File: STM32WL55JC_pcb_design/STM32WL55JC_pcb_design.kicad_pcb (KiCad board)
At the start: 2 copper layers, 98 parts, among them IC1 CY8C9540A-24PVXIT, IC2 PE4259, IC3 HTS221TR, J1 Conn_01x03, J10 Conn_01x06_Male, J11 Conn_02x02_Odd_Even, J12 Conn_01x10, J13 Conn_01x10, J14 Conn_01x10, J15 Conn_01x10, J16 Conn_Coaxial, J17 CT3151-2, J18 CT3151-2, J19 USB_A, J2 Conn_01x03, J20 Conn_02x02_Odd_Even, J21 Conn_01x11_Male, J3 Conn_02x05_Odd_Even, J4 Conn_01x03, J5 Conn_01x09, J6 Conn_01x09, J7 Conn_01x03, J8 Conn_01x09, J9 Conn_01x09, Q1 AO3401A, SW1 SW_MEC_5E, SW2 SW_MEC_5E, U1 STM32WL55JCI7, U2 DS1307+, U3 L80-M39, U4 LIS3DHTR, U6 AMS1117-3.3, U7 AMS1117-5.0, Y1 32MHz, Y2 32.768kHz, Y3 32.768kHz

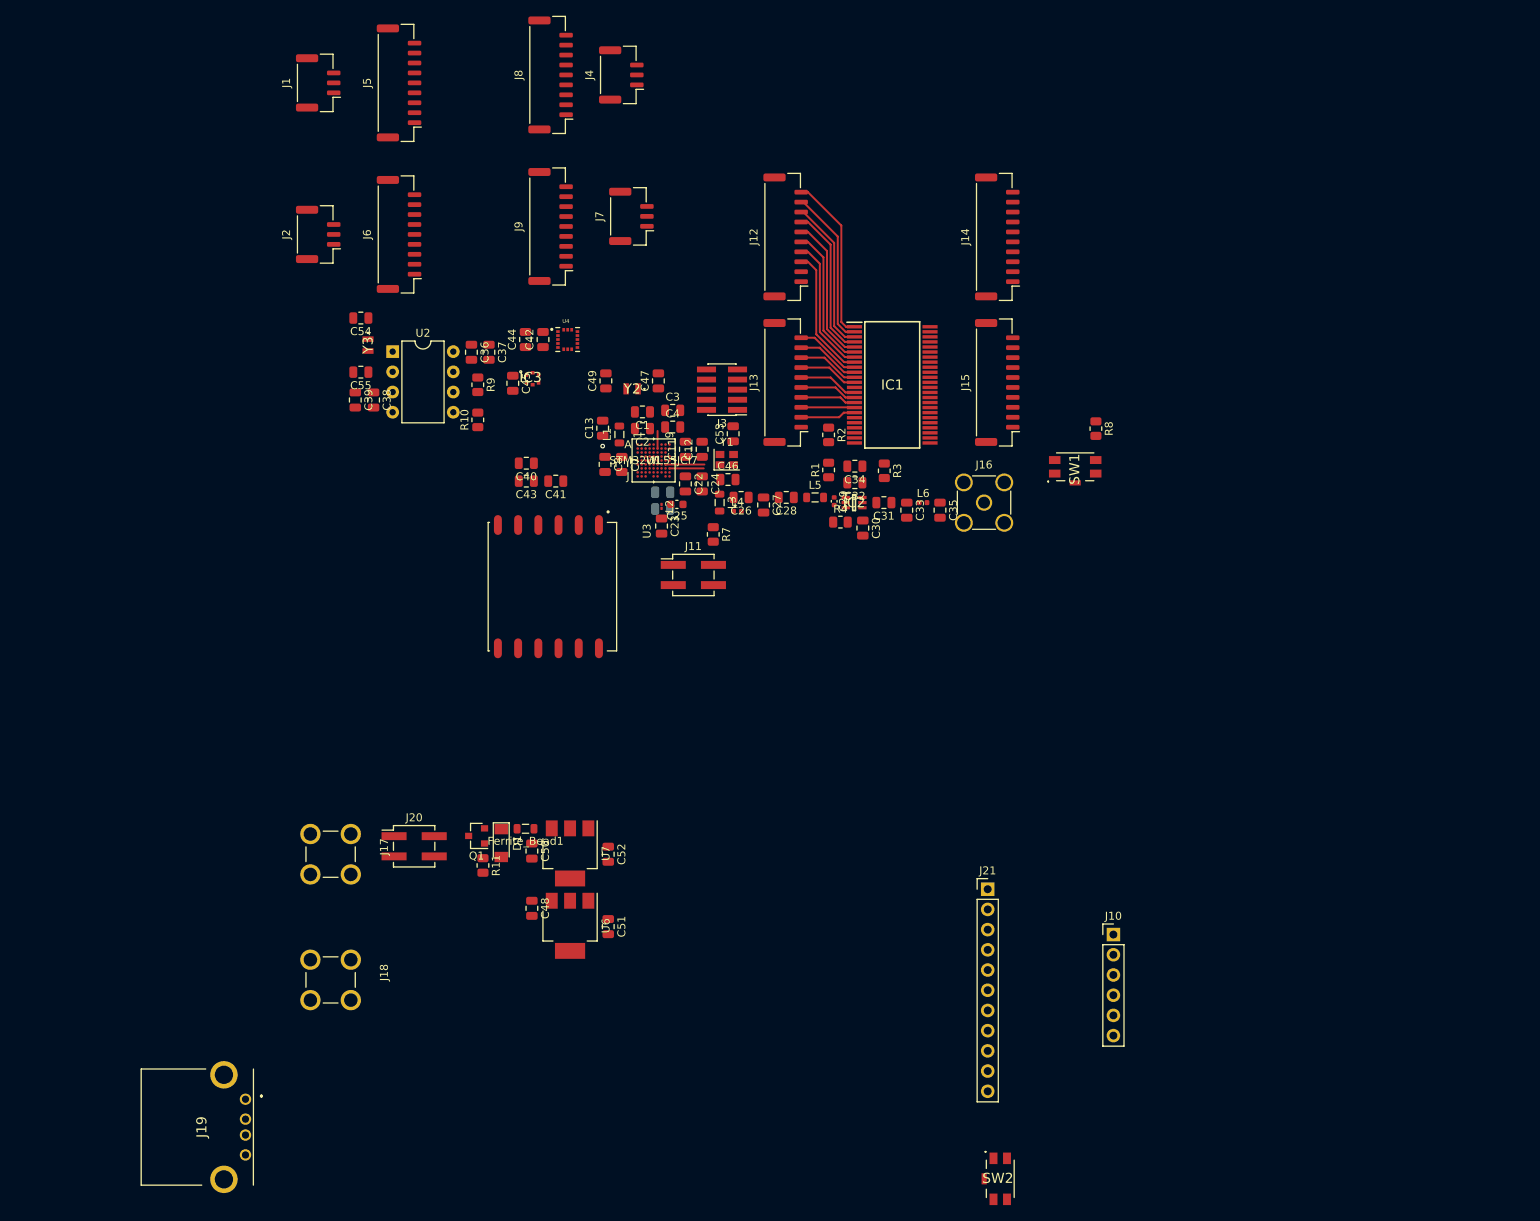
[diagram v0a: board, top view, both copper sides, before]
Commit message: Finished component placement
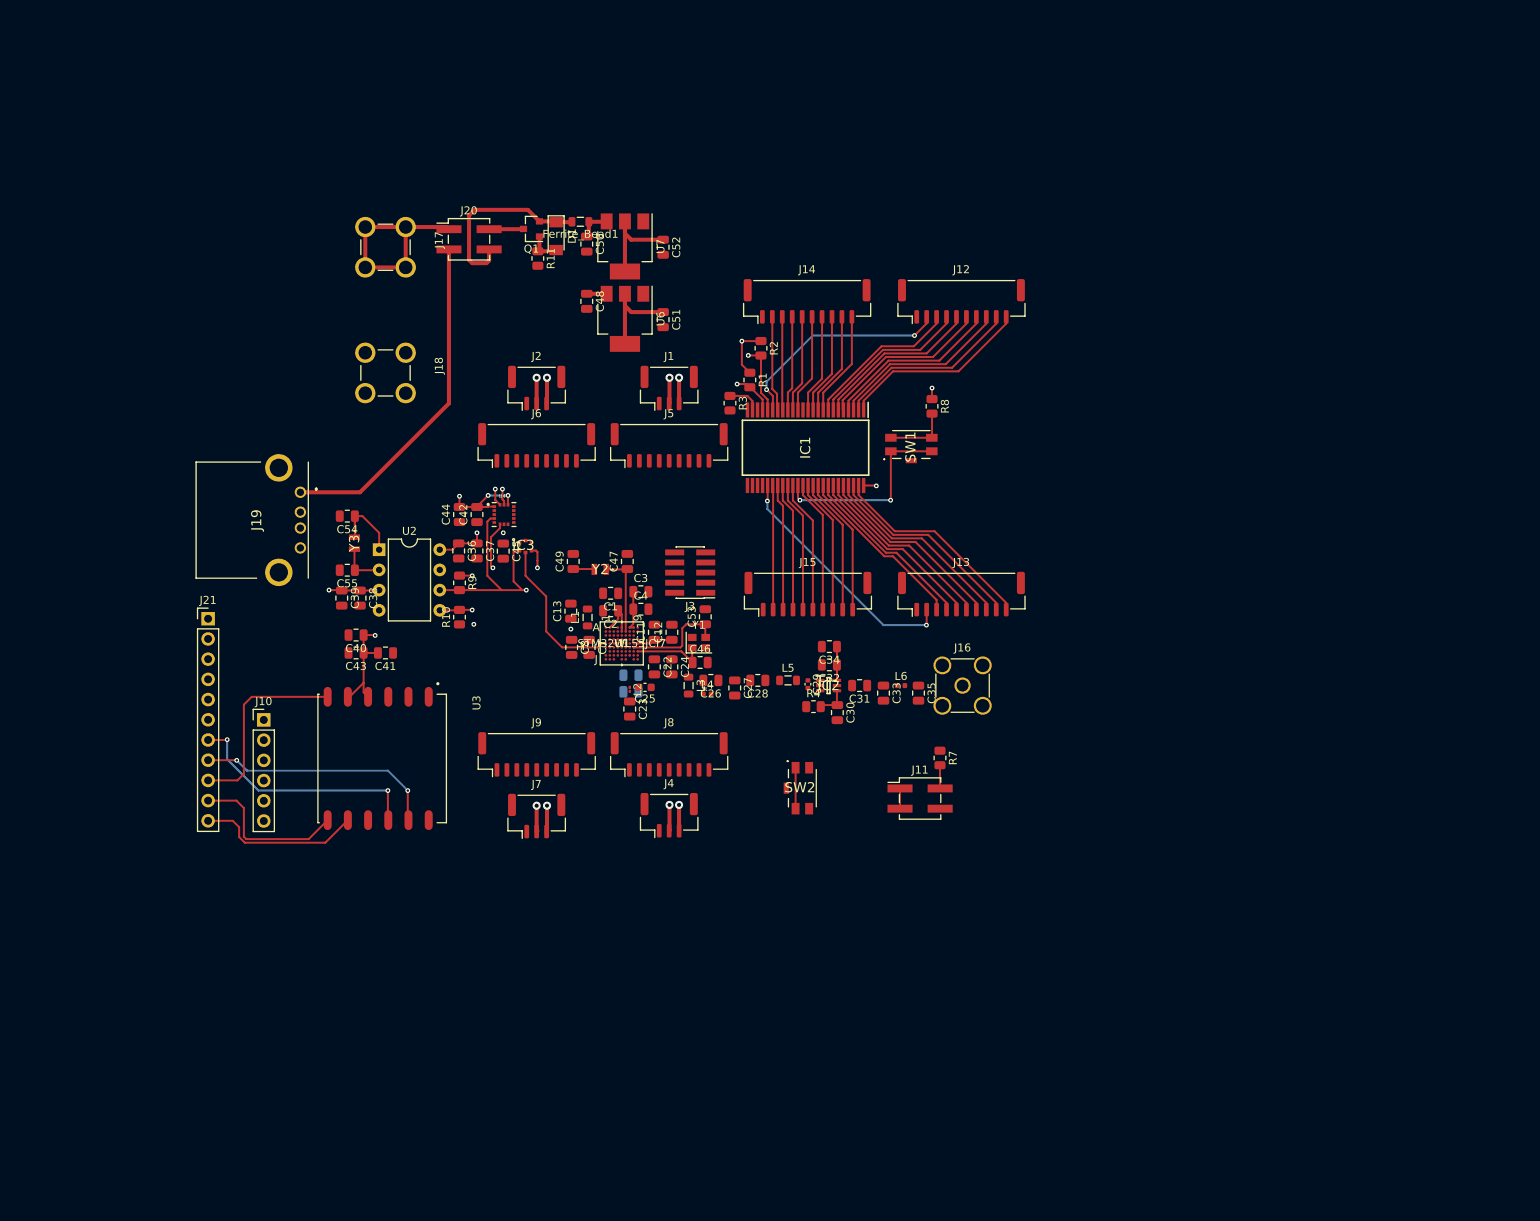
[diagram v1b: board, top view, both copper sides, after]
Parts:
- moved J10 110.2 mm to (110.0, 120.7)
- moved J21 103.7 mm to (103.0, 108.0)
- moved J4 93.3 mm to (161.0, 132.7), turned to 0 degrees
- moved J8 86.7 mm to (161.0, 125.0), turned to 0 degrees
- moved C48 76.6 mm to (150.6, 68.1)
- moved Ferrite_Bead1 76.6 mm to (149.8, 58.1)
- moved J18 76.6 mm to (125.3, 77.1)
- moved J19 76.6 mm to (114.6, 92.1)
- moved Q1 76.6 mm to (143.7, 59.0)
- moved C52 76.6 mm to (160.2, 61.3)
- moved J17 76.6 mm to (125.3, 61.3)
- moved J20 76.6 mm to (135.8, 60.3)
- moved U6 76.6 mm to (155.4, 70.3)
- moved U7 76.6 mm to (155.4, 61.2)
- moved C50 76.6 mm to (150.6, 60.9)
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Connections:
- C36 pad 1: Net-(C36-Pad1) -> 5V
- C37 pad 1: Net-(C36-Pad1) -> 5V
- IC1 pad 10: ENC5_2 -> ENC3_2
- IC1 pad 11: ENC5_3 -> ENC3_3
- IC1 pad 12: ENC5_4 -> ENC3_4
- IC1 pad 14: ENC6_1 -> ENC4_1
- IC1 pad 15: ENC6_2 -> ENC4_2
- IC1 pad 16: ENC6_3 -> ENC4_3
- IC1 pad 17: ENC6_4 -> ENC4_4
- IC1 pad 18: ENC_RST_3 -> ENC_RST_2
- IC1 pad 19: ENC_RST_4 -> ENC_RST_1
- IC1 pad 29: ENC_RST_2 -> ENC_RST_3
- IC1 pad 30: ENC_RST_1 -> ENC_RST_4
- IC1 pad 40: ENC4_4 -> ENC6_4
- IC1 pad 41: ENC4_3 -> ENC6_3
- IC1 pad 42: ENC4_2 -> ENC6_2
- IC1 pad 43: ENC4_1 -> ENC6_1
- IC1 pad 44: ENC3_4 -> ENC5_4
- IC1 pad 45: ENC3_3 -> ENC5_3
- IC1 pad 46: ENC3_2 -> ENC5_2
- IC1 pad 47: ENC3_1 -> ENC5_1
- IC1 pad 9: ENC5_1 -> ENC3_1
- R2 pad 2: EXP_SDA -> EXP_SCL
- SW1 pad 2: Net-(IC1-Pad35) -> Net-(R8-Pad2)
- SW1 pad 3: Net-(R8-Pad2) -> Net-(IC1-Pad35)
- SW2 pad 2: NRST -> GNDREF
- SW2 pad 3: GNDREF -> NRST
- U2 pad 8: Net-(C36-Pad1) -> 5V
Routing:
- net VBAT: track 0.00 -> 89.5 mm, vias 0 -> 15
- net +5V: track 0.00 -> 42.7 mm
- net SDA: track 0.00 -> 34.1 mm, vias 0 -> 3
- net 5V: track 0.00 -> 32.3 mm, vias 0 -> 5
- net GPS_RESET: track 0.00 -> 30.4 mm, vias 0 -> 2
- net GPS_EX_ANT: track 0.00 -> 30.4 mm, vias 0 -> 2
- net ENC_RST_1: track 0.00 -> 27.9 mm, vias 0 -> 2
- net SCL: track 0.00 -> 27.3 mm, vias 0 -> 1
- net Net-(J17-Pad1): track 0.00 -> 25.9 mm
- net Net-(IC1-Pad35): track 0.00 -> 24.7 mm, vias 0 -> 2
- net GPS_1PPS: track 0.00 -> 24.5 mm
- net ENC_RST_3: track 6.94 -> 31.0 mm, vias 0 -> 2
- net Net-(D1-Pad1): track 0.00 -> 23.7 mm
- net GPS_AADET_N: track 0.00 -> 20.6 mm
- net GPS_TIMER: track 0.00 -> 20.1 mm
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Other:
- copper layers 2 -> 4

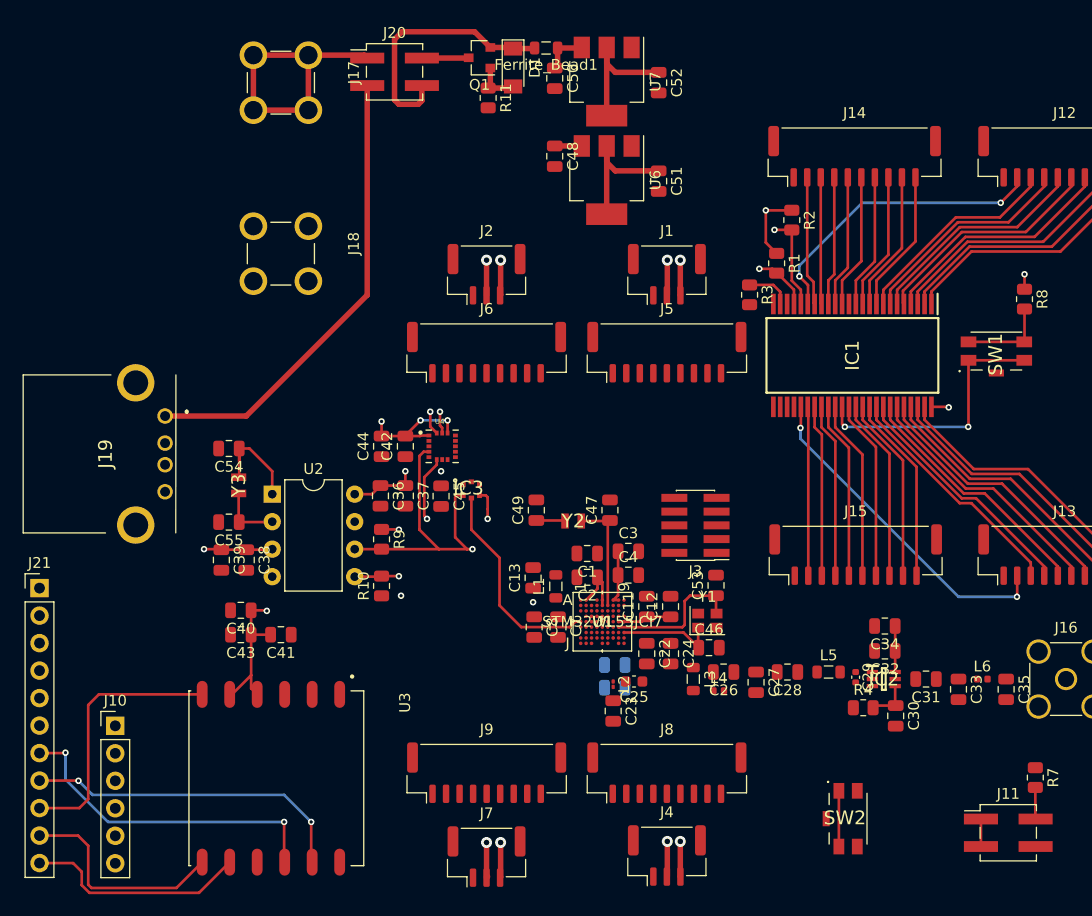
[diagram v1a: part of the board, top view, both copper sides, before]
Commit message: Only micro left to be routed
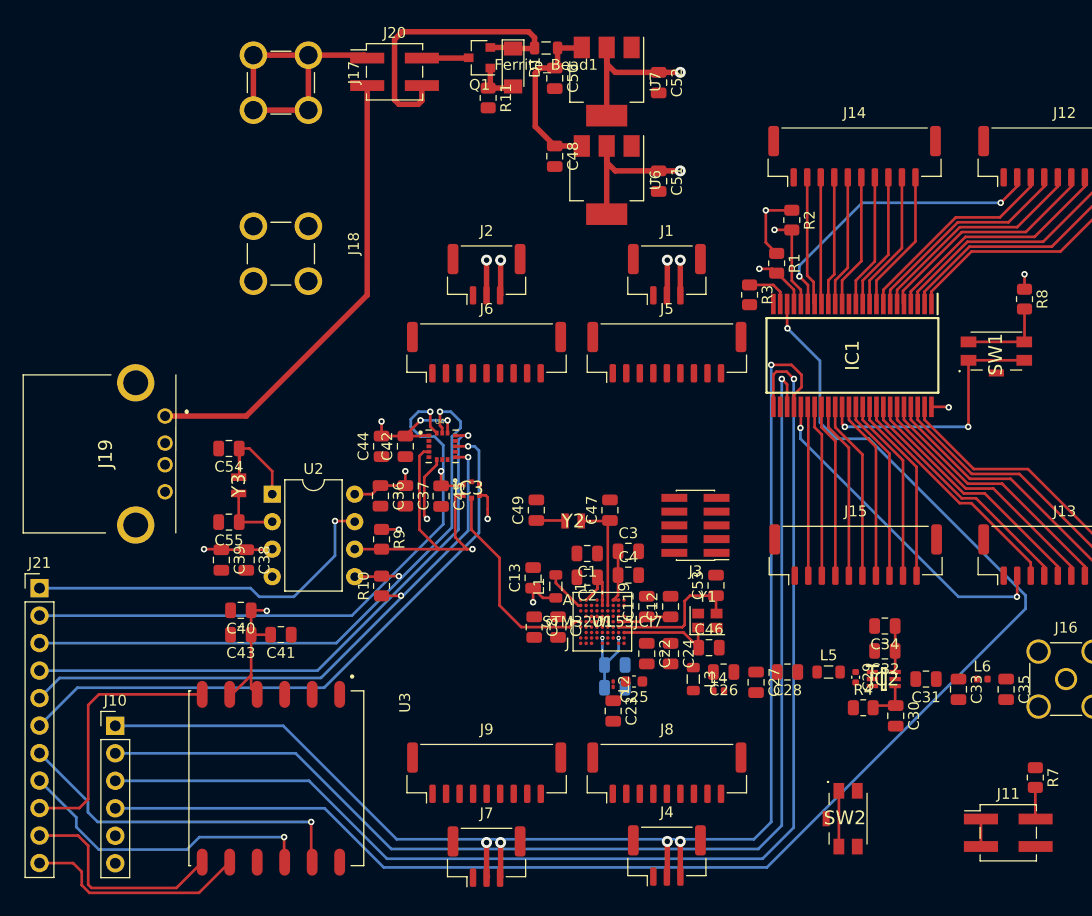
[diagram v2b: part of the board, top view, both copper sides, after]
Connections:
- J21 pad 2: ACC_ADC3 -> ACC_ADC1
- J21 pad 4: ACC_ADC1 -> ACC_ADC3
- J21 pad 7: GPS_RESET -> GPS_EX_ANT
- J21 pad 8: GPS_EX_ANT -> GPS_RESET
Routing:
- net EXP_3: track 0.00 -> 135.3 mm, vias 0 -> 1
- net EXP_0: track 0.00 -> 114.4 mm, vias 0 -> 1
- net EXP_2: track 0.00 -> 113.6 mm, vias 0 -> 1
- net EXP_1: track 0.00 -> 110.2 mm, vias 0 -> 1
- net ACC_INT1: track 0.00 -> 58.0 mm, vias 0 -> 1
- net ACC_ADC2: track 2.06 -> 57.0 mm
- net ACC_ADC3: track 0.00 -> 54.6 mm, vias 0 -> 1
- net ACC_ADC1: track 2.22 -> 56.8 mm
- net ACC_INT2: track 0.00 -> 54.0 mm, vias 0 -> 1
- net RTC_SQW: track 0.00 -> 35.1 mm, vias 0 -> 1
- net VBAT: track 89.5 -> 104.5 mm, vias 15 -> 18
- net Net-(C48-Pad1): track 6.72 -> 16.2 mm
- net Net-(D1-Pad1): track 23.7 -> 28.4 mm
- net Net-(L1-Pad2): track 0.00 -> 3.91 mm
- net VDDRF_1V55: track 0.00 -> 3.77 mm, vias 0 -> 1
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
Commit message: Add some microcontroller routing
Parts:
- moved J4 1.20 mm to (161.0, 133.9)
- moved J7 1.20 mm to (144.3, 134.0)
- moved C23 1.05 mm to (156.9, 118.9), turned to 0 degrees
- moved C7 0.99 mm to (150.1, 112.1)
- moved C8 0.99 mm to (147.8, 112.1)
- moved J8 0.50 mm to (161.0, 124.5)
- moved J9 0.50 mm to (144.3, 124.5)
- moved C25 0.25 mm to (158.1, 116.8)
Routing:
- net RFO_LP: track 0.00 -> 56.9 mm, vias 0 -> 3
- net ADC_SCLK1: track 0.00 -> 53.5 mm, vias 0 -> 2
- net ADC_CNVST2_2: track 0.00 -> 51.0 mm, vias 0 -> 3
- net PC5: track 0.00 -> 49.0 mm, vias 0 -> 5
- net ADC_CNVST1_1: track 0.00 -> 48.3 mm, vias 0 -> 4
- net Net-(J11-Pad1): track 2.54 -> 50.4 mm, vias 0 -> 3
- net ADC_DIN1: track 0.00 -> 47.6 mm
- net ADC_DOUT1: track 0.00 -> 46.1 mm, vias 0 -> 5
- net NRST: track 5.15 -> 50.8 mm, vias 0 -> 7
- net EXP_SCL: track 8.79 -> 52.9 mm, vias 1 -> 4
- net ADC_CNVST1_2: track 0.00 -> 37.0 mm, vias 0 -> 3
- net ADC_CS2_2: track 0.00 -> 36.5 mm, vias 0 -> 2
- net EXP_SDA: track 5.32 -> 41.7 mm, vias 1 -> 2
- net EXP_INT: track 0.00 -> 32.2 mm, vias 0 -> 3
- net RF_CTRL: track 0.00 -> 31.3 mm
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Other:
- rule via_min_drill: 0.2 -> 0.15
- rule via_min_size: 0.4 -> 0.3

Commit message: Finish new design schematic
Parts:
- removed U6: AMS1117-3.3, Package_TO_SOT_SMD:SOT-223-3_TabPin2
- removed U7: AMS1117-5.0, Package_TO_SOT_SMD:SOT-223-3_TabPin2
- added C14: 15pF, Capacitor_SMD:C_0805_2012Metric, F.Cu at (209.0, 142.3)
- added C15: 13pF, Capacitor_SMD:C_0402_1005Metric, F.Cu at (199.0, 152.4)
- added C16: 100nF, Capacitor_SMD:C_0805_2012Metric, F.Cu at (245.3, 114.6)
- added C17: 13pF, Capacitor_SMD:C_0402_1005Metric, F.Cu at (266.7, 103.0)
- added C18: 13pF, Capacitor_SMD:C_0402_1005Metric, F.Cu at (266.7, 101.1)
- added C19: 100nF, Capacitor_SMD:C_0805_2012Metric, F.Cu at (249.7, 111.6)
- added C20: 100nF, Capacitor_SMD:C_0805_2012Metric, F.Cu at (245.3, 117.6)
- added C21: 100nF, Capacitor_SMD:C_0805_2012Metric, F.Cu at (262.3, 99.1)
- added C5: 100nF, Capacitor_SMD:C_0805_2012Metric, F.Cu at (184.2, 164.5)
- added C56: 100nF, Capacitor_SMD:C_0805_2012Metric, F.Cu at (177.5, 111.4)
- added C57: 10uF, Capacitor_SMD:C_0805_2012Metric, F.Cu at (181.9, 108.3)
- added C58: 100nF, Capacitor_SMD:C_0805_2012Metric, F.Cu at (177.5, 105.3)
- added C59: 10uF, Capacitor_SMD:C_0805_2012Metric, F.Cu at (192.8, 96.6)
- added C6: 4.7uF, Capacitor_SMD:C_0805_2012Metric, F.Cu at (204.6, 145.3)
- added C60: 100nF, Capacitor_SMD:C_0805_2012Metric, F.Cu at (186.4, 103.8)
- added C61: 10uF, Capacitor_SMD:C_0805_2012Metric, F.Cu at (128.7, 56.8)
- added C62: 10uF, Capacitor_SMD:C_0805_2012Metric, F.Cu at (128.7, 47.7)
- added C63: 10uF, Capacitor_SMD:C_0805_2012Metric, F.Cu at (138.5, 60.0)
- added C64: 10uF, Capacitor_SMD:C_0805_2012Metric, F.Cu at (138.5, 50.9)
- added IC4: PE4259, PE4259:SOT65P210X110-6N, F.Cu at (244.4, 96.4)
- added IC5: PE4259, PE4259:SOT65P210X110-6N, F.Cu at (236.0, 104.7)
- added IC6: HTS221TR, HTS221TR:HTS221TR, F.Cu at (121.0, 73.0)
- added L10: 4.7nH, Inductor_SMD:L_0805_2012Metric, F.Cu at (231.9, 117.5)
- added L11: 18nH, Inductor_SMD:L_0805_2012Metric, F.Cu at (240.7, 104.2)
- added L7: 22nH, Inductor_SMD:L_0805_2012Metric, F.Cu at (240.7, 107.0)
- added L8: 5.6nH, Inductor_SMD:L_0805_2012Metric, F.Cu at (236.0, 110.7)
- added L9: 12nH, Inductor_SMD:L_0805_2012Metric, F.Cu at (245.2, 102.4)
- added R12: 100kOhm, Resistor_SMD:R_0805_2012Metric, F.Cu at (122.0, 52.3)
- added R13: 0R, Resistor_SMD:R_0805_2012Metric, F.Cu at (249.7, 117.5)
- added R14: 0R, Resistor_SMD:R_0805_2012Metric, F.Cu at (258.5, 108.0)
- added R15: 0R, Resistor_SMD:R_0805_2012Metric, F.Cu at (254.0, 108.5)
- added R5: 1k, Resistor_SMD:R_0805_2012Metric, F.Cu at (205.8, 108.4)
- added R6: 0R, Resistor_SMD:R_0805_2012Metric, F.Cu at (258.5, 105.1)
- added U5: AMS1117-5.0, Package_TO_SOT_SMD:SOT-223-3_TabPin2, F.Cu at (133.6, 49.9)
- added Y4: 32.768kHz, SC20S-12.5PF20PPM:SC20S125PF20PPM, F.Cu at (177.9, 101.6)
- C10, C9: moved to F.Cu
- C11, C3: value 100nF -> 4.7uF
- C12: value 100nF -> 13pF; footprint Capacitor_SMD:C_0805_2012Metric -> Capacitor_SMD:C_0402_1005Metric
- C13: value 470nF -> 15pF
- C22: value 47nF -> 47pF
- C23: value 1.8pF -> 100nF
- C24: value 47pF -> 10nF
- C25: value 2.4pF -> 8.2pF
- C26: value 3.3pF -> 100pF
- C27: value 5.6pF -> 8.2pF; footprint Capacitor_SMD:C_0805_2012Metric -> Capacitor_SMD:C_0603_1608Metric
- C28: value 39pF -> 47pF
- C29: value 2.2pF -> 22pF; footprint Capacitor_SMD:C_0402_1005Metric -> Capacitor_SMD:C_0805_2012Metric
- C30: value 1nF -> 47pF
- C31: value 39pF -> 3.3pF; footprint Capacitor_SMD:C_0805_2012Metric -> Capacitor_SMD:C_0402_1005Metric
- C32, C41, C45: value 100nF -> 47pF
- C33: value 3.3pF -> 47pF
- C34, C50, C52: value 10uF -> 15pF
- C35: value 3.3pF -> 8.2pF; footprint Capacitor_SMD:C_0805_2012Metric -> Capacitor_SMD:C_0603_1608Metric
- C36: value 100nF -> 2.7pF; footprint Capacitor_SMD:C_0805_2012Metric -> Capacitor_SMD:C_0603_1608Metric
- C37: value 10uF -> 1.5pF; footprint Capacitor_SMD:C_0805_2012Metric -> Capacitor_SMD:C_0402_1005Metric
- C38: value 100nF -> 12pF
- C39: value 10uF -> 3.3pF; footprint Capacitor_SMD:C_0805_2012Metric -> Capacitor_SMD:C_0402_1005Metric
- C40: value 100nF -> 47nF
- C42: value 100nF -> 4.7pF; footprint Capacitor_SMD:C_0805_2012Metric -> Capacitor_SMD:C_0603_1608Metric
- C43, C44, C48: value 10uF -> 1nF
- C46: value 2.2pF -> 1nF
- C47: value 15pF -> 47pF
- C49, C55: value 15pF -> 100nF
- C53: value 2.2pF -> 100nF
- C54: value 15pF -> 10uF
- C7: value 100nF -> 10nF
- C8: value 100nF -> 1uF
- IC1: value CY8C9540A-24PVXIT -> STM32F051R8T6; footprint CY8C9540A-24PVXIT:SOP64P1035X279-48N -> STM32F051R8T6:QFP50P1200X1200X160-64N
- IC2: value PE4259 -> CY8C9540A-24PVXIT; footprint PE4259:SOT65P210X110-6N -> CY8C9540A-24PVXIT:SOP64P1035X279-48N
- IC3: value HTS221TR -> SX1276IMLTRT; footprint HTS221TR:HTS221TR -> SX1276IMLTRT:QFN65P600X600X100-29N
- J10: value Conn_01x06_Male -> Conn_02x15_Odd_Even; footprint Connector_PinHeader_2.54mm:PinHeader_1x06_P2.54mm_Vertical -> Connector_PinHeader_2.54mm:PinHeader_2x15_P2.54mm_Vertical
- J17: value CT3151-2 -> Conn_Coaxial; footprint CT3151-2:CALTEST_CT3151-2 -> Connector_Coaxial:SMA_Amphenol_901-144_Vertical
- J19: value USB_A -> CT3151-2; footprint USBASFBTH:USBASFBTH -> CT3151-2:CALTEST_CT3151-2
- J20: value Conn_02x02_Odd_Even -> USB_A; footprint Connector_PinHeader_2.54mm:PinHeader_2x02_P2.54mm_Vertical_SMD -> USBASFBTH:USBASFBTH
- J21: value Conn_01x11_Male -> Conn_02x02_Odd_Even; footprint Connector_PinHeader_2.54mm:PinHeader_1x11_P2.54mm_Vertical -> Connector_PinHeader_2.54mm:PinHeader_2x02_P2.54mm_Vertical_SMD
- J3: value Conn_02x05_Odd_Even -> Conn_01x03; footprint Connector_PinHeader_1.27mm:PinHeader_2x05_P1.27mm_Vertical_SMD -> Connector_JST:JST_GH_BM03B-GHS-TBT_1x03-1MP_P1.25mm_Vertical
- J4, J7: value Conn_01x03 -> Conn_01x09; footprint Connector_JST:JST_GH_BM03B-GHS-TBT_1x03-1MP_P1.25mm_Vertical -> Connector_JST:JST_GH_BM09B-GHS-TBT_1x09-1MP_P1.25mm_Vertical
- J6: value Conn_01x09 -> Conn_01x03; footprint Connector_JST:JST_GH_BM09B-GHS-TBT_1x09-1MP_P1.25mm_Vertical -> Connector_JST:JST_GH_BM03B-GHS-TBT_1x03-1MP_P1.25mm_Vertical
- J9: value Conn_01x09 -> Conn_02x10_Odd_Even; footprint Connector_JST:JST_GH_BM09B-GHS-TBT_1x09-1MP_P1.25mm_Vertical -> Connector_PinHeader_2.54mm:PinHeader_2x10_P2.54mm_Vertical
- L1: value 15uH -> 2.2nH
- L2: value 15nH -> 18nH; footprint Inductor_SMD:L_01005_0402Metric -> Inductor_SMD:L_0805_2012Metric
- L4: value 2.5nH -> 33nH; footprint Inductor_SMD:L_0402_1005Metric -> Inductor_SMD:L_0805_2012Metric
- L5: value 4.7nH -> 4.7pH
- L6: value 9.1nH -> 10nH
- R1, R9: value 2.2k -> 1k
- R11: value 100kOhm -> 2.2k
- R3: value 200 -> 2.2k
- R4: value 100 -> 200
- R7: value 1k -> 0R
- U1: value STM32WL55JCI7 -> DS1307+; footprint MCU_ST_STM3255JCI7:STM32WL55JCI7 -> Package_DIP:DIP-8_W7.62mm
- U2: value DS1307+ -> L80-M39; footprint Package_DIP:DIP-8_W7.62mm -> L80-M39:XCVR_L80-M39
- U3: value L80-M39 -> LIS3DHTR; footprint L80-M39:XCVR_L80-M39 -> LIS3DHTR:XDCR_LIS3DHTR
- U4: value LIS3DHTR -> AMS1117-3.3; footprint LIS3DHTR:XDCR_LIS3DHTR -> Package_TO_SOT_SMD:SOT-223-3_TabPin2
- Y1: footprint Oscillator:Oscillator_SMD_SeikoEpson_SG210-4Pin_2.5x2.0mm -> NX2016SA32MEXS00ACS06465:NX2016SA32MEXS00ACS06465
- Y3: value 32.768kHz -> 32MHz; footprint SC20S-12.5PF20PPM:SC20S125PF20PPM -> NX2016SA32MEXS00ACS06465:NX2016SA32MEXS00ACS06465
- moved C39 142.3 mm to (262.1, 107.1), turned to 0 degrees
- moved C42 126.3 mm to (262.7, 104.8), turned to 0 degrees
- moved C41 124.8 mm to (249.7, 102.6), turned to 0 degrees
- moved C37 121.5 mm to (257.4, 114.0), turned to 0 degrees
- moved R9 119.8 mm to (254.1, 111.5), turned to 0 degrees
- moved C40 118.9 mm to (240.5, 109.9), turned to 0 degrees
- moved C43 114.8 mm to (236.4, 116.6), turned to 0 degrees
- moved C38 114.6 mm to (236.4, 113.6), turned to 0 degrees
- moved C45 113.3 mm to (253.4, 99.1), turned to 0 degrees
- moved C44 111.4 mm to (245.2, 108.3), turned to 0 degrees
- moved C48 111.0 mm to (258.0, 96.1), turned to 0 degrees
- moved J17 110.4 mm to (229.0, 99.2), turned to 0 degrees
- moved C36 109.7 mm to (240.9, 72.5), turned to 0 degrees
- moved Y3 106.9 mm to (226.9, 115.8), turned to 0 degrees
- moved L1 98.5 mm to (248.9, 99.7), turned to 0 degrees
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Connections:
- C1 pad 1: VBAT -> VDD
- C10 pad 1: VBAT -> VDD
- C11 pad 1: VBAT -> VDD
- C12 pad 1: VBAT -> OSC_IN
- C13 pad 1: VDDRF_1V55 -> OSC32_IN
- C2 pad 1: VBAT -> VDD
- C22 pad 1: VR_PA -> VDD
- C23 pad 1: RFI_P -> VDD
- C24 pad 1: VR_PA -> Net-(C24-Pad1)
- C25 pad 2: RFI_N -> GNDREF
- C26 pad 1: Net-(C26-Pad1) -> Net-(C24-Pad1)
- C26 pad 2: RFO_HP -> GNDREF
- C27 pad 1: Net-(C26-Pad1) -> Net-(C27-Pad1)
- C28 pad 2: Net-(C26-Pad1) -> Net-(C25-Pad1)
- C29 pad 2: GNDREF -> Net-(C27-Pad1)
- C3 pad 1: VBAT -> VDD
- C30 pad 1: Net-(C30-Pad1) -> Net-(C24-Pad1)
- C31 pad 2: Net-(C31-Pad2) -> GNDREF
- C32 pad 1: VBAT -> Net-(C32-Pad1)
- C32 pad 2: GNDREF -> Net-(C32-Pad2)
- C33 pad 1: Net-(C31-Pad1) -> Net-(C33-Pad1)
- C33 pad 2: GNDREF -> Net-(C31-Pad1)
- C34 pad 1: VBAT -> Net-(C34-Pad1)
- C36 pad 1: 5V -> Net-(C36-Pad1)
- C36 pad 2: GNDREF -> Net-(C34-Pad1)
- C37 pad 1: 5V -> Net-(C37-Pad1)
- C37 pad 2: GNDREF -> Net-(C35-Pad1)
- C38 pad 1: VBAT -> Net-(C36-Pad1)
- C39 pad 1: VBAT -> Net-(C37-Pad1)
- C4 pad 1: VBAT -> VDD
- C40 pad 1: VBAT -> Net-(C40-Pad1)
- C40 pad 2: GNDREF -> Net-(C40-Pad2)
- C41 pad 1: GNDREF -> Net-(C41-Pad1)
- C41 pad 2: VBAT -> Net-(C41-Pad2)
- C42 pad 1: GNDREF -> Net-(C42-Pad1)
- C42 pad 2: VBAT -> GNDREF
- C43 pad 1: VBAT -> Net-(C43-Pad1)
- C44 pad 1: GNDREF -> Net-(C44-Pad1)
- C44 pad 2: VBAT -> GNDREF
- C45 pad 1: VBAT -> Net-(C45-Pad1)
- C45 pad 2: GNDREF -> Net-(C45-Pad2)
- C46 pad 1: OSC_IN -> VDD
- C47 pad 1: OSC32_IN -> Net-(C47-Pad1)
- C47 pad 2: GNDREF -> Net-(C47-Pad2)
- C48 pad 1: Net-(C48-Pad1) -> VDD
- C49 pad 1: OSC32_OUT -> 5V
- C50 pad 1: Net-(C48-Pad1) -> Net-(C50-Pad1)
- C51 pad 1: VBAT -> 5V
- C52 pad 1: 5V -> Net-(C52-Pad1)
- C53 pad 1: OSC_OUT -> VDD
- C54 pad 1: Net-(C54-Pad1) -> VDD
- C55 pad 1: Net-(C55-Pad1) -> VDD
- C7 pad 1: VBAT -> VDD
- C8 pad 1: VBAT -> VDD
- C9 pad 1: VBAT -> VDD
- Ferrite_Bead1 pad 1: Net-(C48-Pad1) -> Net-(C61-Pad1)
- IC1 pad 1: ENC1_1 -> VDD
- IC1 pad 10: ENC3_2 -> ADC_CNVST1_2
- IC1 pad 11: ENC3_3 -> ADC_CNVST2_1
- IC1 pad 12: ENC3_4 -> GNDREF
- IC1 pad 13: GNDREF -> VDD
- IC1 pad 14: ENC4_1 -> ADC_CNVST2_2
- IC1 pad 15: ENC4_2 -> ADC_CNVST3_1
- IC1 pad 16: ENC4_3 -> ADC_CNVST3_2
- IC1 pad 17: ENC4_4 -> ADC_CS1_1
- IC1 pad 18: ENC_RST_2 -> ADC_CS1_2
- IC1 pad 19: ENC_RST_1 -> ADC_CS2_1
- IC1 pad 2: ENC1_2 -> PC13
- IC1 pad 20: EXP_SCL -> ADC_CS2_2
- IC1 pad 21: EXP_SDA -> ADC_SCLK
- IC1 pad 22: EXP_3 -> ADC_DOUT
- IC1 pad 23: Net-(IC1-Pad23) -> ADC_DIN
- IC1 pad 24: GNDREF -> ADC_CS3_1
- IC1 pad 25: EXP_2 -> ADC_CS3_2
- IC1 pad 26: EXP_INT -> ADC_CS4_1
- IC1 pad 27: EXP_1 -> ADC_CS4_2
- IC1 pad 28: EXP_0 -> ADC_CNVST4_1
- IC1 pad 29: ENC_RST_3 -> ADC_CNVST4_2
- IC1 pad 3: ENC1_3 -> OSC32_IN
- IC1 pad 30: ENC_RST_4 -> LoRa_RXTX_CTRL
- IC1 pad 31: ENC8_4 -> GNDREF
- IC1 pad 32: ENC8_3 -> VDD
- IC1 pad 33: ENC8_2 -> LoRa_NSS
- IC1 pad 34: ENC8_1 -> LoRa_SCK
- IC1 pad 35: Net-(IC1-Pad35) -> LoRa_MISO
- IC1 pad 36: ENC7_4 -> LoRa_MOSI
- IC1 pad 37: ENC7_3 -> LoRa_DO5
- IC1 pad 38: ENC7_2 -> LoRa_DO4
- IC1 pad 39: ENC7_1 -> LoRa_DO3
- IC1 pad 4: ENC1_4 -> OSC32_OUT
- IC1 pad 40: ENC6_4 -> LoRa_DO2
- IC1 pad 41: ENC6_3 -> LoRa_DO1
- IC1 pad 42: ENC6_2 -> LoRa_DO0
- IC1 pad 43: ENC6_1 -> LoRa_NRST
- IC1 pad 44: ENC5_4 -> PA11
- IC1 pad 45: ENC5_3 -> EXP_INT
- IC1 pad 46: ENC5_2 -> SWDIO
- IC1 pad 47: ENC5_1 -> EXP_SCL
- IC1 pad 48: VBAT -> EXP_SDA
- IC1 pad 5: ENC2_1 -> OSC_IN
- IC1 pad 6: ENC2_2 -> OSC_OUT
- IC1 pad 7: ENC2_3 -> NRST
- IC1 pad 8: ENC2_4 -> PC0
- IC1 pad 9: ENC3_1 -> ADC_CNVST1_1
- IC2 pad 1: Net-(C29-Pad1) -> ENC1_1
- IC2 pad 2: GNDREF -> ENC1_2
- IC2 pad 3: Net-(C25-Pad1) -> ENC1_3
- IC2 pad 4: Net-(C30-Pad1) -> ENC1_4
- IC2 pad 5: Net-(C31-Pad2) -> ENC2_1
- IC2 pad 6: VBAT -> ENC2_2
- IC3 pad 1: VBAT -> Net-(IC3-Pad1)
- IC3 pad 2: SCL -> Net-(C20-Pad1)
- IC3 pad 3: TempHumid_DRDY -> VDD
- IC3 pad 4: SDA -> Net-(C21-Pad1)
- IC3 pad 5: GNDREF -> Net-(C18-Pad1)
- IC3 pad 6: Net-(IC3-Pad6) -> Net-(C17-Pad1)
- J1 pad 2: VBAT -> VDD
- J10 pad 1: EXP_0 -> PA11
- J10 pad 2: EXP_1 -> ACC_ADC1
- J10 pad 3: EXP_2 -> PB3
- J10 pad 4: EXP_3 -> ACC_ADC2
- J10 pad 5: PC5 -> PB4
- J10 pad 6: RFO_LP -> ACC_ADC3
- J11 pad 1: Net-(J11-Pad1) -> BOOT0
- J11 pad 3: Net-(J11-Pad1) -> BOOT0
- J16 pad 1: Net-(C35-Pad1) -> Net-(J16-Pad1)
- J17 pad 2: Net-(J17-Pad1) -> GNDREF
- J18 pad 1: GNDREF -> Net-(J18-Pad1)
- J18 pad 2: GNDREF -> Net-(J18-Pad1)
- J18 pad 3: GNDREF -> Net-(J18-Pad1)
- J18 pad 4: GNDREF -> Net-(J18-Pad1)
- J19 pad 1: +5V -> GNDREF
- J19 pad 2: Net-(J19-Pad2) -> GNDREF
- J19 pad 3: Net-(J19-Pad3) -> GNDREF
- J2 pad 2: VBAT -> VDD
- J20 pad 1: Net-(J17-Pad1) -> +5V
- J20 pad 3: +5V -> Net-(J20-Pad3)
- J20 pad 4: Net-(D1-Pad1) -> GNDREF
- J21 pad 1: RTC_SQW -> Net-(J18-Pad1)
- J21 pad 2: ACC_ADC1 -> Net-(J21-Pad2)
- J21 pad 3: ACC_ADC2 -> +5V
- J21 pad 4: ACC_ADC3 -> Net-(D1-Pad1)
- J3 pad 1: VBAT -> GNDREF
- J3 pad 2: SWDIO -> VDD
- J3 pad 3: GNDREF -> 5V
- J4 pad 1: GNDREF -> ADC_CNVST1_2
- J4 pad 2: VBAT -> ADC_CS1_2
- J4 pad 3: 5V -> ADC_EOC1_2
- J5 pad 1: ADC_CNVST1_2 -> ADC_CNVST2_2
- J5 pad 2: ADC_CS1_2 -> ADC_CS2_2
- J5 pad 3: ADC_EOC1_2 -> ADC_EOC2_2
- J5 pad 4: ADC_CNVST1_1 -> ADC_CNVST2_1
- J5 pad 5: ADC_CS1_1 -> ADC_CS2_1
- J5 pad 6: ADC_SCLK1 -> ADC_SCLK
- J5 pad 7: ADC_DIN1 -> ADC_DIN
- J5 pad 8: ADC_DOUT1 -> ADC_DOUT
- J5 pad 9: ADC_EOC1_1 -> ADC_EOC2_1
- J6 pad 1: ADC_CNVST2_2 -> GNDREF
- J6 pad 2: ADC_CS2_2 -> VDD
- J6 pad 3: ADC_EOC2_2 -> 5V
- J7 pad 1: GNDREF -> ADC_CNVST3_2
- J7 pad 2: VBAT -> ADC_CS3_2
- J7 pad 3: 5V -> ADC_EOC3_2
- J8 pad 1: ADC_CNVST3_2 -> ADC_CNVST4_2
- J8 pad 2: ADC_CS3_2 -> ADC_CS4_2
- J8 pad 3: ADC_EOC3_2 -> ADC_EOC4_2
- J8 pad 4: ADC_CNVST3_1 -> ADC_CNVST4_1
- J8 pad 5: ADC_CS3_1 -> ADC_CS4_1
- J8 pad 6: ADC_SCLK2 -> ADC_SCLK
- J8 pad 7: ADC_DIN2 -> ADC_DIN
- J8 pad 8: ADC_DOUT2 -> ADC_DOUT
- J8 pad 9: ADC_EOC3_1 -> ADC_EOC4_1
- J9 pad 1: ADC_CNVST4_2 -> VDD
- J9 pad 2: ADC_CS4_2 -> VDD
- J9 pad 3: ADC_EOC4_2 -> GNDREF
- J9 pad 4: ADC_CNVST4_1 -> GNDREF
- J9 pad 5: ADC_CS4_1 -> GNDREF
- J9 pad 6: ADC_SCLK2 -> GNDREF
- J9 pad 7: ADC_DIN2 -> SWDIO
- J9 pad 8: ADC_DOUT2 -> GNDREF
- J9 pad 9: ADC_EOC4_1 -> SWCLK
- L1 pad 1: VDDRF_1V55 -> Net-(C27-Pad1)
- L1 pad 2: Net-(L1-Pad2) -> Net-(IC3-Pad27)
- L2 pad 1: RFI_N -> GNDREF
- L2 pad 2: RFI_P -> Net-(IC3-Pad1)
- L3 pad 1: VR_PA -> Net-(C24-Pad1)
- L3 pad 2: RFO_HP -> Net-(C25-Pad1)
- L4 pad 1: RFO_HP -> Net-(C27-Pad1)
- L4 pad 2: Net-(C26-Pad1) -> Net-(C24-Pad1)
- L5 pad 1: Net-(C28-Pad1) -> Net-(IC3-Pad1)
- L5 pad 2: Net-(C29-Pad1) -> Net-(C32-Pad2)
- L6 pad 1: Net-(C31-Pad1) -> Net-(IC3-Pad21)
- L6 pad 2: Net-(C35-Pad1) -> Net-(C31-Pad1)
- Q1 pad 3: Net-(J20-Pad2) -> Net-(J21-Pad2)
- R1 pad 1: VBAT -> VDD
- R1 pad 2: EXP_SDA -> Net-(J11-Pad2)
- R10 pad 1: VBAT -> VDD
- R10 pad 2: SDA -> SCL
- R11 pad 1: Net-(D1-Pad2) -> VDD
- R11 pad 2: GNDREF -> SDA
- R2 pad 1: VBAT -> VDD
- R2 pad 2: EXP_SCL -> EXP_SDA
- R3 pad 1: Net-(IC1-Pad23) -> VDD
- R3 pad 2: GNDREF -> EXP_SCL
- R4 pad 1: RF_CTRL -> Net-(IC2-Pad23)
- R4 pad 2: Net-(C30-Pad1) -> GNDREF
- R7 pad 1: VBAT -> Net-(C33-Pad1)
- R7 pad 2: Net-(J11-Pad2) -> Net-(C41-Pad2)
- R8 pad 1: VBAT -> LoRa_RXTX_CTRL
- R8 pad 2: Net-(R8-Pad2) -> Net-(C43-Pad1)
- R9 pad 1: VBAT -> LoRa_RXTX_CTRL
- R9 pad 2: SCL -> Net-(C44-Pad1)
- SW1 pad 1: Net-(IC1-Pad35) -> Net-(SW1-Pad1)
- SW1 pad 2: Net-(R8-Pad2) -> Net-(SW1-Pad2)
- SW1 pad 3: Net-(IC1-Pad35) -> Net-(SW1-Pad3)
- SW1 pad 4: Net-(R8-Pad2) -> GNDREF
- SW2 pad 1: NRST -> Net-(IC2-Pad35)
- SW2 pad 2: GNDREF -> Net-(R5-Pad2)
- SW2 pad 3: NRST -> Net-(IC2-Pad35)
- SW2 pad 4: GNDREF -> Net-(R5-Pad2)
- U2 pad 1: Net-(C54-Pad1) -> RX
- U2 pad 2: Net-(C55-Pad1) -> TX
- U2 pad 3: VBAT -> GNDREF
- U2 pad 4: GNDREF -> VDD
- U2 pad 5: SDA -> VDD
- U2 pad 6: SCL -> GPS_1PPS
- U2 pad 7: RTC_SQW -> GPS_TIMER
- U2 pad 8: 5V -> GPS_AADET_N
- U3 pad 1: RX -> VDD
- U3 pad 10: GPS_RESET -> GNDREF
- U3 pad 11: GPS_EX_ANT -> ACC_INT1
- U3 pad 2: TX -> (no net)
- U3 pad 3: GNDREF -> (no net)
- U3 pad 4: VBAT -> SCL
- U3 pad 5: VBAT -> GNDREF
- U3 pad 6: GPS_1PPS -> SDA
- U3 pad 7: GPS_TIMER -> Net-(U3-Pad7)
- U3 pad 8: GPS_AADET_N -> Net-(U3-Pad8)
- U3 pad 9: (no net) -> ACC_INT2
- U4 pad 1: VBAT -> GNDREF
- U4 pad 2: (no net) -> VDD
- U4 pad 3: (no net) -> Net-(C61-Pad1)
- Y3 pad 1: Net-(C54-Pad1) -> Net-(C17-Pad1)
- Y3 pad 2: Net-(C55-Pad1) -> GNDREF
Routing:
- net VBAT: track 118.3 -> 0.00 mm, vias 28 -> 0
- net EXP_0: track 114.4 -> 0.00 mm, vias 1 -> 0
- net EXP_2: track 113.6 -> 0.00 mm, vias 1 -> 0
- net EXP_1: track 110.2 -> 0.00 mm, vias 1 -> 0
- net EXP_3: track 106.1 -> 0.00 mm, vias 1 -> 0
- net ACC_INT1: track 58.0 -> 0.00 mm, vias 1 -> 0
- net ACC_ADC2: track 57.0 -> 0.00 mm, vias 1 -> 0
- net RFO_LP: track 56.9 -> 0.00 mm, vias 3 -> 0
- net ACC_ADC1: track 56.8 -> 0.00 mm, vias 1 -> 0
- net ACC_ADC3: track 54.6 -> 0.00 mm, vias 1 -> 0
- net ACC_INT2: track 54.0 -> 0.00 mm, vias 1 -> 0
- net ADC_SCLK1: track 53.5 -> 0.00 mm, vias 2 -> 0
- net EXP_SCL: track 52.9 -> 0.00 mm, vias 4 -> 0
- net ADC_CNVST2_2: track 51.0 -> 0.00 mm, vias 3 -> 0
- net NRST: track 50.8 -> 0.00 mm, vias 7 -> 0
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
